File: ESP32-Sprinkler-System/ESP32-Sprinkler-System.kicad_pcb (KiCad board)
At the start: 2 copper layers, 135 x 87 mm, 62 parts, among them J101 12V, J102 DHT, J103 NEOPIXEL, J104 LCD, J105 BME280, J201 TBL004-508-02BE-2GY, J202 TBL004-508-02BE-2GY, J203 TBL004-508-02BE-2GY, J204 TBL004-508-02BE-2GY, Q201 IRFZ24NPBF, Q202 IRFZ24NPBF, Q203 IRFZ24NPBF, Q204 IRFZ24NPBF, U101 V7805-500, U102 ESP32-DEVKITC-32D, U201 MC33152PG, U202 MC33152PG

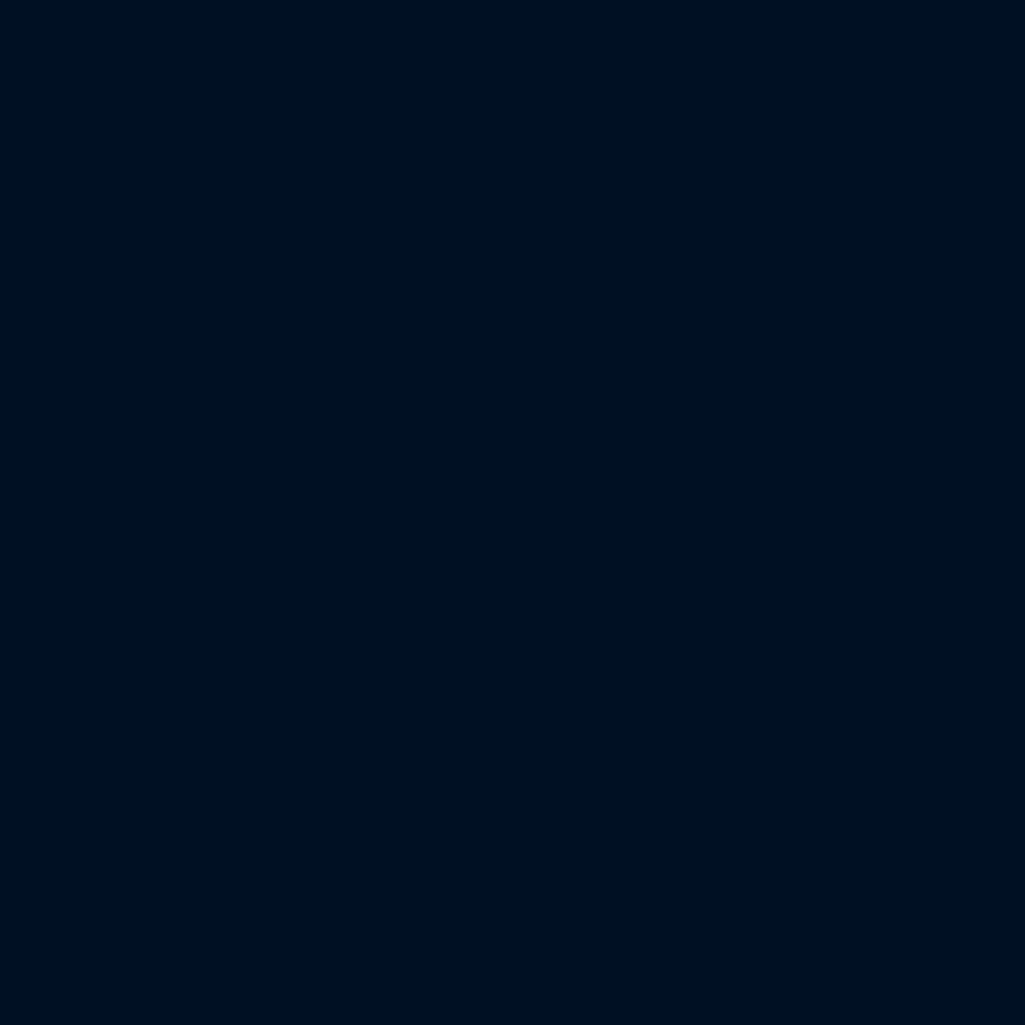
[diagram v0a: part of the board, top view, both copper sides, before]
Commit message: making new pcb 120x120mm
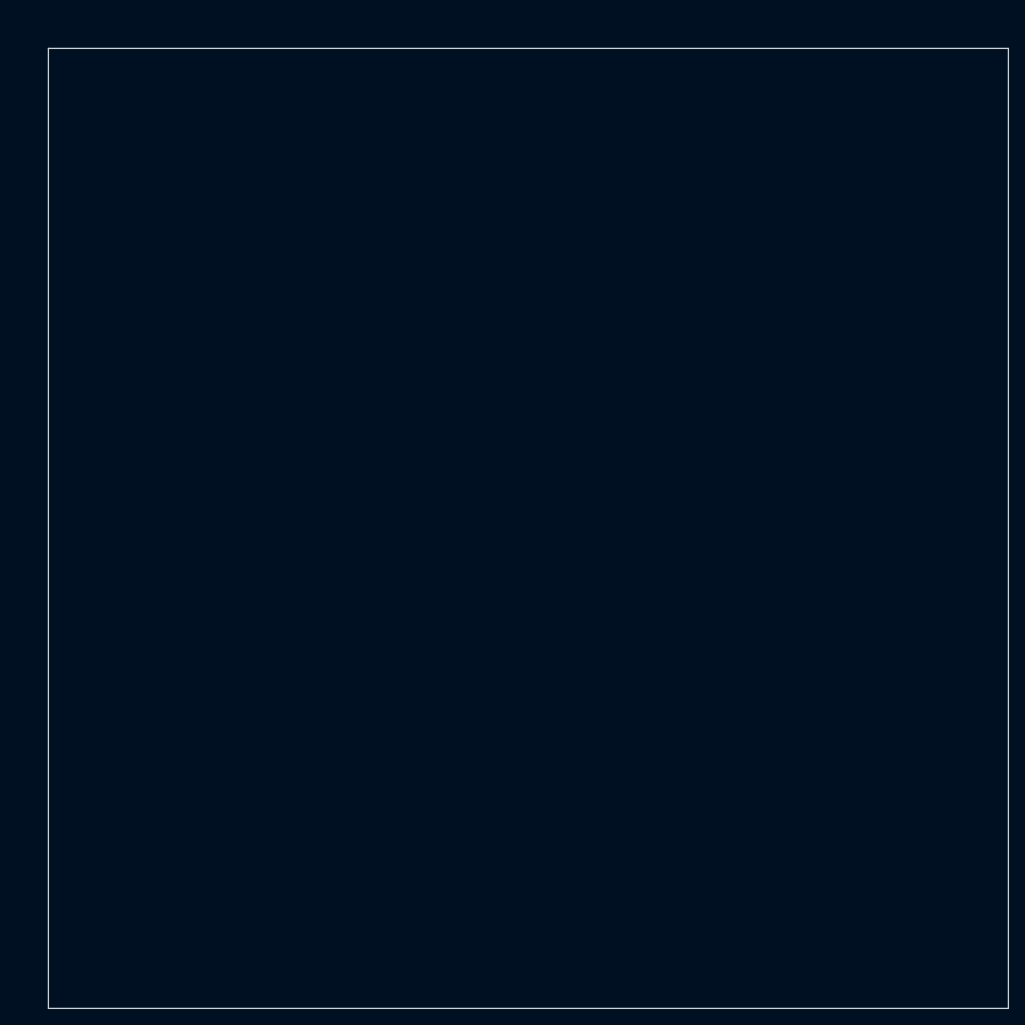
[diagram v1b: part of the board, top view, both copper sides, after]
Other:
- board size 135 x 87 mm -> 355 x 221 mm
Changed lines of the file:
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@@
   (gr_arc (start 58 57) (mid 59.171573 54.171573) (end 62 53) (layer "Edge.Cuts") (width 0.2))
   (gr_line (start 189 53) (end 62 53) (layer "Edge.Cuts") (width 0.2))
+  (gr_rect (start 293 154) (end 413 274) (layer "Edge.Cuts") (width 0.1) (fill none))
   (gr_line (start 62 140) (end 189 140) (layer "Edge.Cuts") (width 0.2))
   (gr_line (start 58 57) (end 58 136) (layer "Edge.Cuts") (width 0.2))

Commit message: new layout most in pos some traces ran
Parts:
- moved H103 163.4 mm to (195.0, 41.0), turned to 90 degrees
- moved H102 143.0 mm to (83.0, 153.0), turned to 90 degrees
- moved C103 82.0 mm to (185.8, 125.4), turned to 90 degrees
- moved J201 80.8 mm to (93.5, 143.6), turned to 0 degrees
- moved J204 79.9 mm to (146.9, 143.6), turned to 0 degrees
- moved J101 75.5 mm to (177.3, 143.3)
- moved D202 75.5 mm to (92.2, 138.6), turned to 0 degrees
- moved Q204 73.9 mm to (158.2, 130.0), turned to 180 degrees
- moved D208 72.7 mm to (145.6, 138.6), turned to 0 degrees
- moved J202 72.2 mm to (111.3, 143.6), turned to 0 degrees
- moved J203 71.9 mm to (129.1, 143.6), turned to 0 degrees
- moved U101 70.8 mm to (188.5, 136.5), turned to 90 degrees
- moved R201 70.0 mm to (93.5, 134.7), turned to 0 degrees
- moved C104 69.0 mm to (179.5, 124.2), turned to 90 degrees
- moved R216 68.9 mm to (146.8, 134.7), turned to 0 degrees
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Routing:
- net 3.3V: track 114.6 -> 32.6 mm
- net SW_A: track 78.7 -> 0.00 mm
- net DHT: track 69.0 -> 0.00 mm, vias 2 -> 0
- net MOSI: track 54.9 -> 0.00 mm
- net SCK: track 49.5 -> 0.00 mm
- net BACKLIGHT: track 32.4 -> 0.00 mm
- net D/C: track 32.1 -> 0.00 mm
- net 12V: track 262.6 -> 294.7 mm
- net SDA: track 31.8 -> 0.00 mm
- net CS: track 28.7 -> 0.00 mm
- net SCL: track 20.0 -> 0.00 mm
- net NEOPIXEL: track 16.5 -> 0.00 mm
- net 5V: track 63.5 -> 71.6 mm
- net Net-(R208-Pad1): track 15.8 -> 22.3 mm, vias 1 -> 0
- net Net-(D205-Pad1): track 5.50 -> 0.00 mm
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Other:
- board size 355 x 221 mm -> 352 x 235 mm
- board text added: "Rev.2"

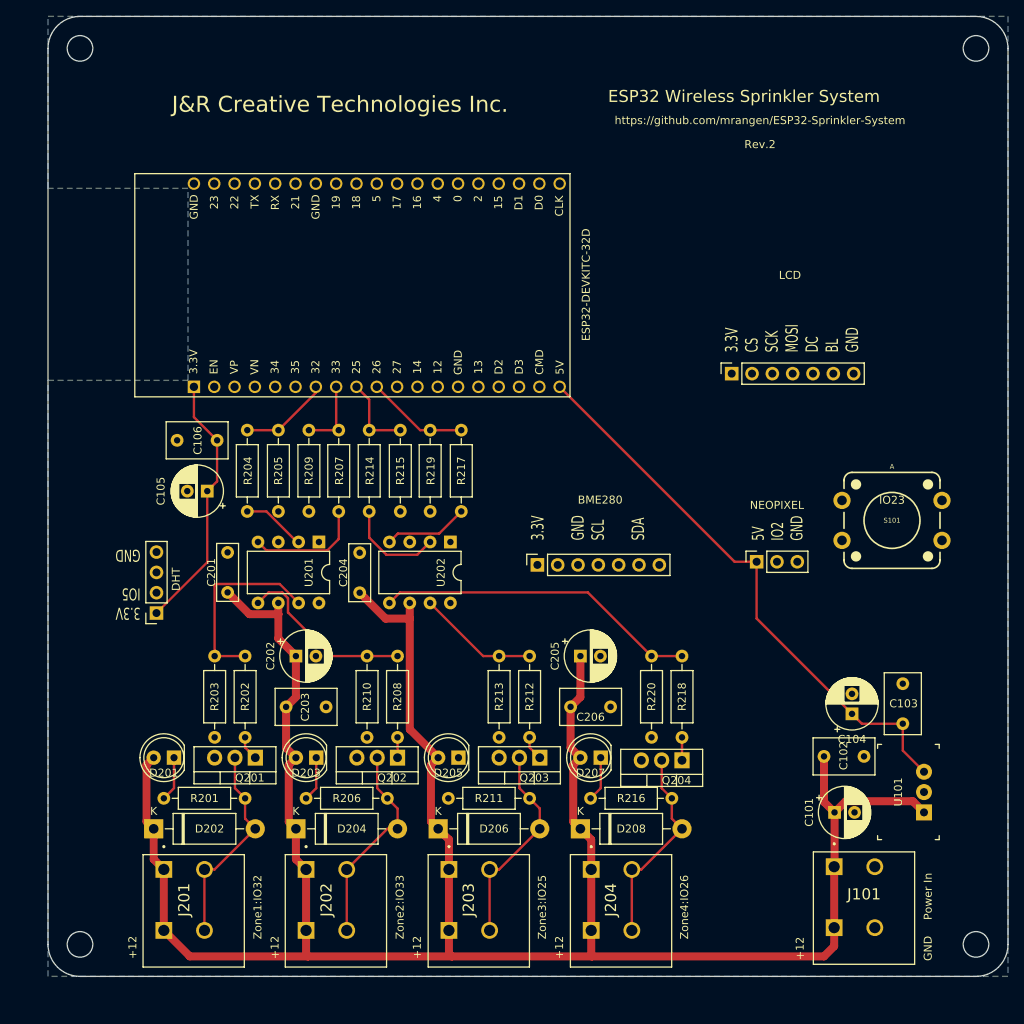
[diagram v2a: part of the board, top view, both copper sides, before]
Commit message: 4 new mount holes
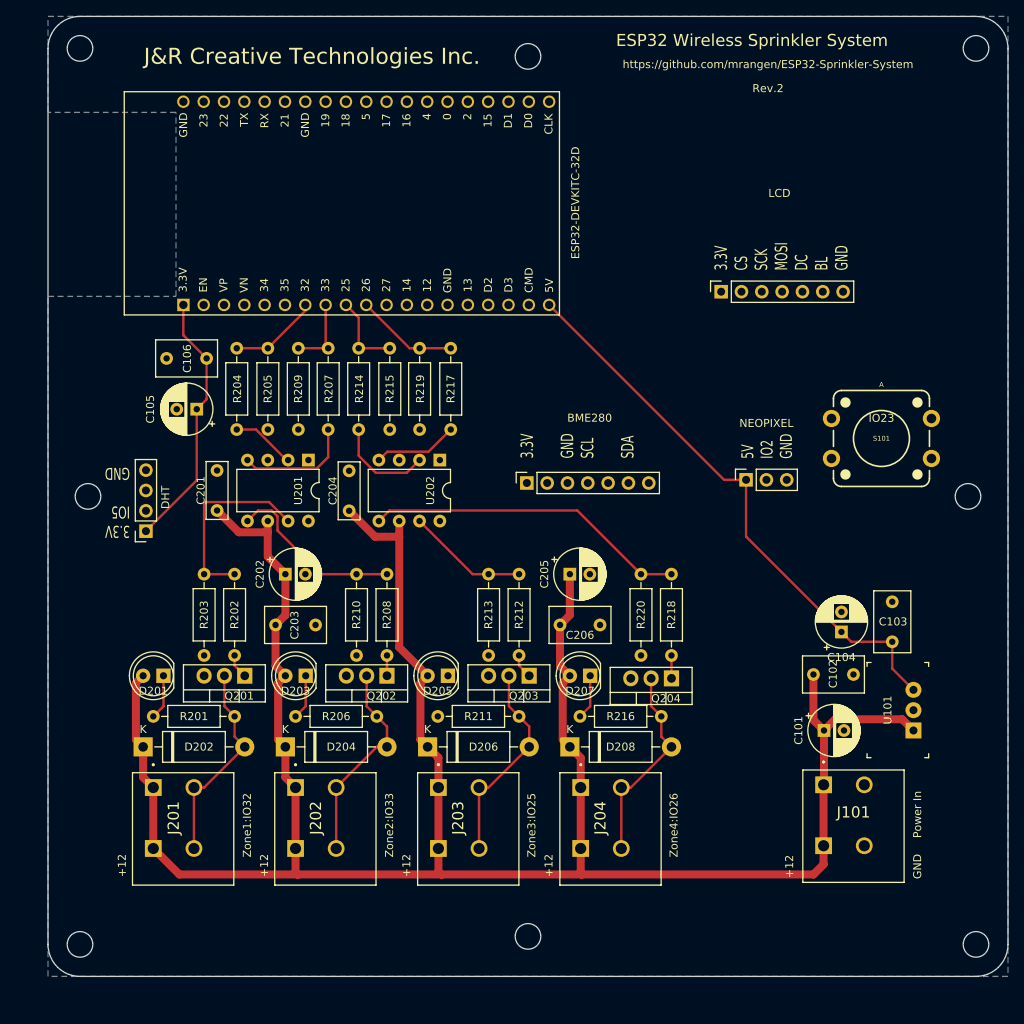
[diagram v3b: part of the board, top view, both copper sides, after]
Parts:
- added H104: MountingHole, MountingHole:MountingHole_3.2mm_M3, F.Cu at (139.0, 152.0)
- added H104: MountingHole, MountingHole:MountingHole_3.2mm_M3, F.Cu at (139.0, 42.0)
- added H104: MountingHole, MountingHole:MountingHole_3.2mm_M3, F.Cu at (194.0, 97.0)
- added H104: MountingHole, MountingHole:MountingHole_3.2mm_M3, F.Cu at (84.0, 97.0)
- moved Q204 10.3 mm to (156.9, 119.7)
- moved R201 10.3 mm to (92.2, 124.5)
- moved R206 10.3 mm to (109.9, 124.5)
- moved R216 10.3 mm to (145.5, 124.5)
- moved R211 10.3 mm to (127.7, 124.5)
- moved U102 10.3 mm to (115.7, 60.4)
- moved C101 10.3 mm to (176.0, 126.3)
- moved C102 10.3 mm to (174.7, 119.3)
- moved C103 10.3 mm to (184.5, 115.2)
- moved C104 10.3 mm to (178.2, 113.9)
- moved C106 10.3 mm to (98.8, 79.8)
- moved C201 10.3 mm to (100.1, 98.8)
- moved C203 10.3 mm to (107.4, 113.1)
- moved C205 10.3 mm to (144.2, 106.7)
- moved C206 10.3 mm to (143.0, 113.1)
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
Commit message: Update ESP32-Sprinkler-System.kicad_pcb
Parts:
- moved J101 0.24 mm to (176.0, 133.3)
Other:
- board size 352 x 235 mm -> 120 x 120 mm

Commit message: proper fit in box now
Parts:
- moved J103 12.5 mm to (174.9, 104.0)
- moved S101 8.45 mm to (177.0, 84.0)
- moved C101 6.68 mm to (169.3, 126.3)
- moved C102 6.68 mm to (168.0, 119.3)
- moved C103 6.68 mm to (177.8, 115.2)
- moved C104 6.68 mm to (171.5, 113.9)
- moved J101 6.68 mm to (169.3, 133.3)
- moved U101 6.68 mm to (180.5, 126.3)
- moved J105 4.29 mm to (142.5, 97.7)
- moved J102 3.76 mm to (95.0, 101.3)
- moved U102 2.72 mm to (115.0, 63.0)
- moved J104 1.80 mm to (162.3, 73.0)
- moved C105 0.44 mm to (97.6, 86.5)
- moved C106 0.44 mm to (98.8, 80.2)
- moved R204 0.44 mm to (102.6, 78.9)
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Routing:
- net 5V: track 71.6 -> 14.0 mm
- net 3.3V: track 32.6 -> 0.00 mm
- net Net-(R207-Pad2): track 14.6 -> 0.00 mm
- net Net-(R214-Pad2): track 12.4 -> 0.00 mm
- net Net-(R217-Pad2): track 10.6 -> 0.00 mm
- net 12V: track 294.7 -> 284.6 mm
- net Net-(R204-Pad2): track 8.00 -> 0.00 mm
- net Net-(D205-Pad1): track 0.00 -> 5.61 mm
- net Valve1: track 11.2 -> 9.22 mm
- net Valve3: track 9.96 -> 8.05 mm
- net Valve2: track 9.28 -> 7.37 mm
- net Net-(R202-Pad1): track 24.2 -> 25.4 mm
- net Net-(R218-Pad1): track 40.4 -> 41.0 mm
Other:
- board text added: "PCB: 120mm x 120mm Holes: 110mm x 110mm"

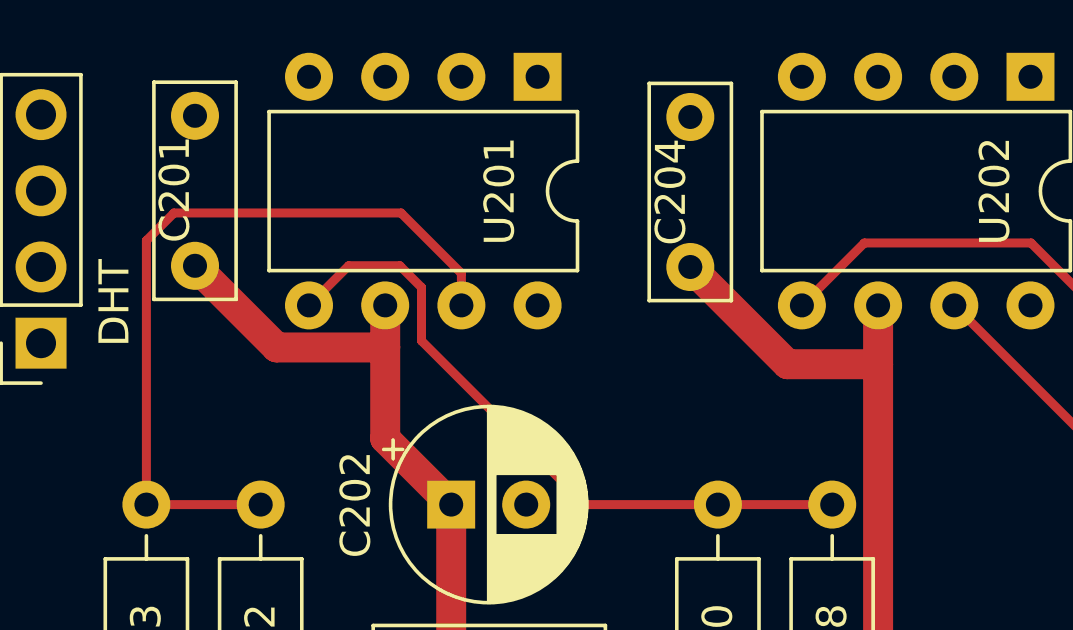
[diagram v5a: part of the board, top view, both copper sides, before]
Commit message: Added comments to PCB in UserComments layer.
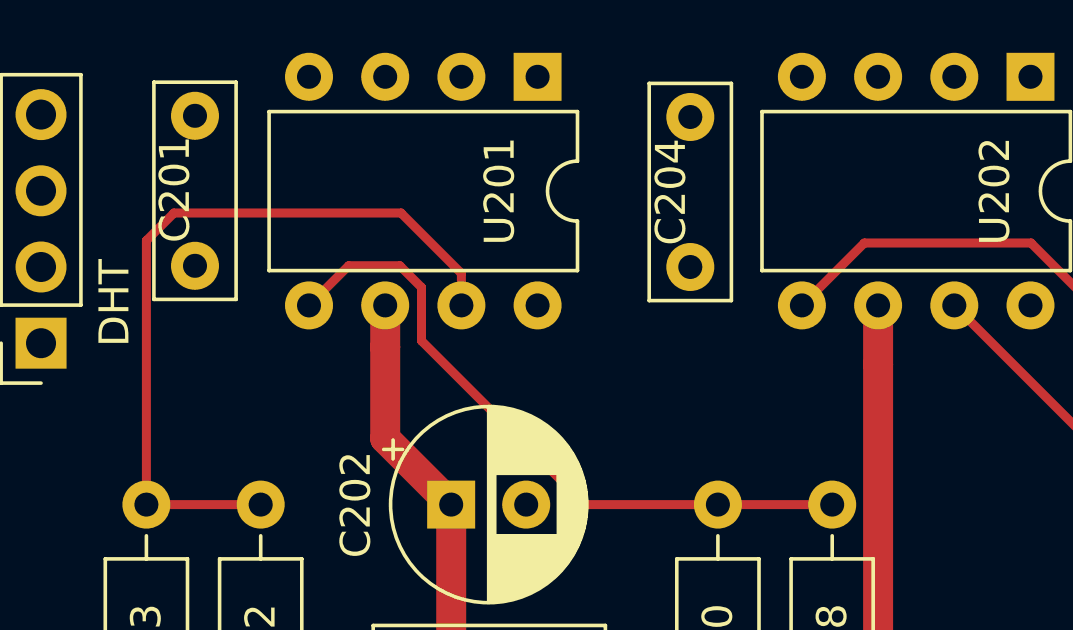
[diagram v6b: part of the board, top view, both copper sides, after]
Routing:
- net 12V: track 284.6 -> 269.6 mm
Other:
- board text added: "Decoupling capacitor placement looks good."
- board text added: "Power traces to and from the terminal blocks should have traces of equal thickness."
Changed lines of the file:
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@@
+    (effects (font (size 1 1) (thickness 0.15)))
+  )
+  (gr_text "Decoupling capacitor placement looks good." (at 127.23 180.96) (layer "Cmts.User")
+    (effects (font (size 1 1) (thickness 0.15)))
+  )
+  (gr_text "Power traces to and from the\nterminal blocks should have\ntraces of equal thickness." (at 100.67 171.05) (layer "Cmts.User")
     (effects (font (size 1 1) (thickness 0.15)))
   )
@@
   (segment (start 145.58238 133.39012) (end 145.58238 129.66012) (width 1) (layer "F.Cu") (net 5))
   (segment (start 169.31762 133) (end 169.27 133.04762) (width 1) (layer "F.Cu") (net 5))
-  (segment (start 116.64238 98.80012) (end 119.88238 102.04012) (width 1) (layer "F.Cu") (net 5))
   (segment (start 145.58238 143.58238) (end 145.78933 143.78933) (width 1) (layer "F.Cu") (net 5))
   (segment (start 145.58238 129.66012) (end 144.23238 128.31012) (width 1) (layer "F.Cu") (net 5))
@@
   (segment (start 127.80238 133.39012) (end 127.80238 141.01012) (width 1) (layer "F.Cu") (net 5))
   (segment (start 127.78933 143.78933) (end 145.78933 143.78933) (width 1) (layer "F.Cu") (net 5))
-  (segment (start 100.13238 98.76012) (end 102.85238 101.48012) (width 1) (layer "F.Cu") (net 5))
   (segment (start 108.67238 132.12012) (end 109.94238 133.39012) (width 1) (layer "F.Cu") (net 5))
   (segment (start 94.94159 143.78933) (end 109.78933 143.78933) (width 1) (layer "F.Cu") (net 5))
@@
   (segment (start 144.23238 119.42012) (end 143.33238 120.32012) (width 1) (layer "F.Cu") (net 5))
   (segment (start 169.31762 126.26012) (end 169.31762 133) (width 1) (layer "F.Cu") (net 5))
-  (segment (start 102.85238 101.48012) (end 106.46238 101.48012) (width 1) (layer "F.Cu") (net 5))
   (segment (start 125.55238 127.41012) (end 126.45238 128.31012) (width 1) (layer "F.Cu") (net 5))
   (segment (start 89.99238 127.41012) (end 90.89238 128.31012) (width 1) (layer "F.Cu") (net 5))
@@
   (segment (start 90.89238 128.31012) (end 90.89238 132.12012) (width 1) (layer "F.Cu") (net 5))
   (segment (start 106.47238 104.52012) (end 108.67238 106.72012) (width 1) (layer "F.Cu") (net 5))
-  (segment (start 119.88238 102.04012) (end 122.90238 102.04012) (width 1) (layer "F.Cu") (net 5))
   (segment (start 106.47238 101.47012) (end 106.47238 104.52012) (width 1) (layer "F.Cu") (net 5))
   (segment (start 179.1 124.86012) (end 170.71762 124.86012) (width 1) (layer "F.Cu") (net 5))
@@
   (segment (start 143.33238 120.32012) (end 143.33238 127.41012) (width 1) (layer "F.Cu") (net 5))
   (segment (start 170.71762 124.86012) (end 169.31762 126.26012) (width 1) (layer "F.Cu") (net 5))
-  (segment (start 106.46238 101.48012) (end 106.47238 101.47012) (width 1) (layer "F.Cu") (net 5))
   (segment (start 107.77238 120.32012) (end 107.77238 127.41012) (width 1) (layer "F.Cu") (net 5))
   (segment (start 127.80238 133.39012) (end 127.80238 129.66012) (width 1) (layer "F.Cu") (net 5))
